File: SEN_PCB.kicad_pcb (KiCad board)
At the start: 2 copper layers, 42.5 x 58.7 mm, 8 parts, among them J1 47080-4005, U1 BME680, U2 ADT7310

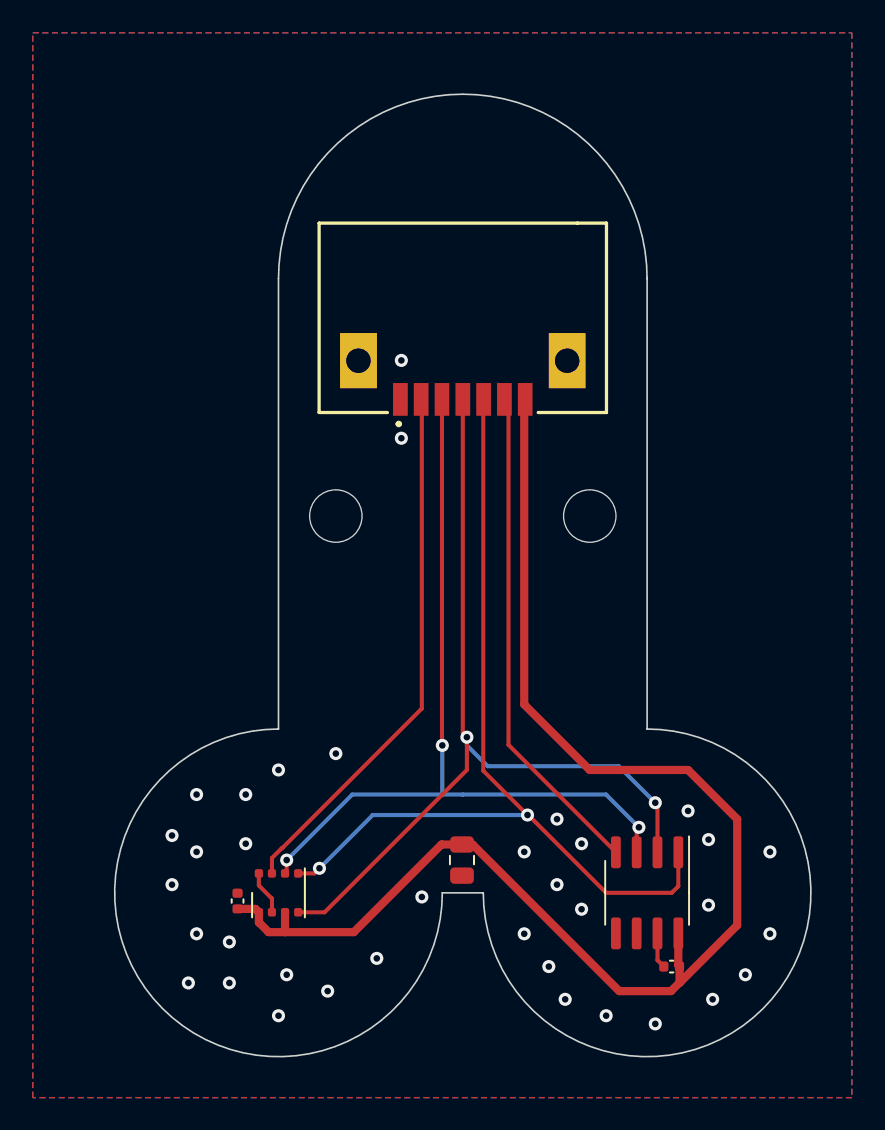
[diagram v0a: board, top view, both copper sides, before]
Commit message: 1V KiCad
Changed form-factor to more appropriate one.
Changed connector pinout meaning to match new pinout on MCU board.
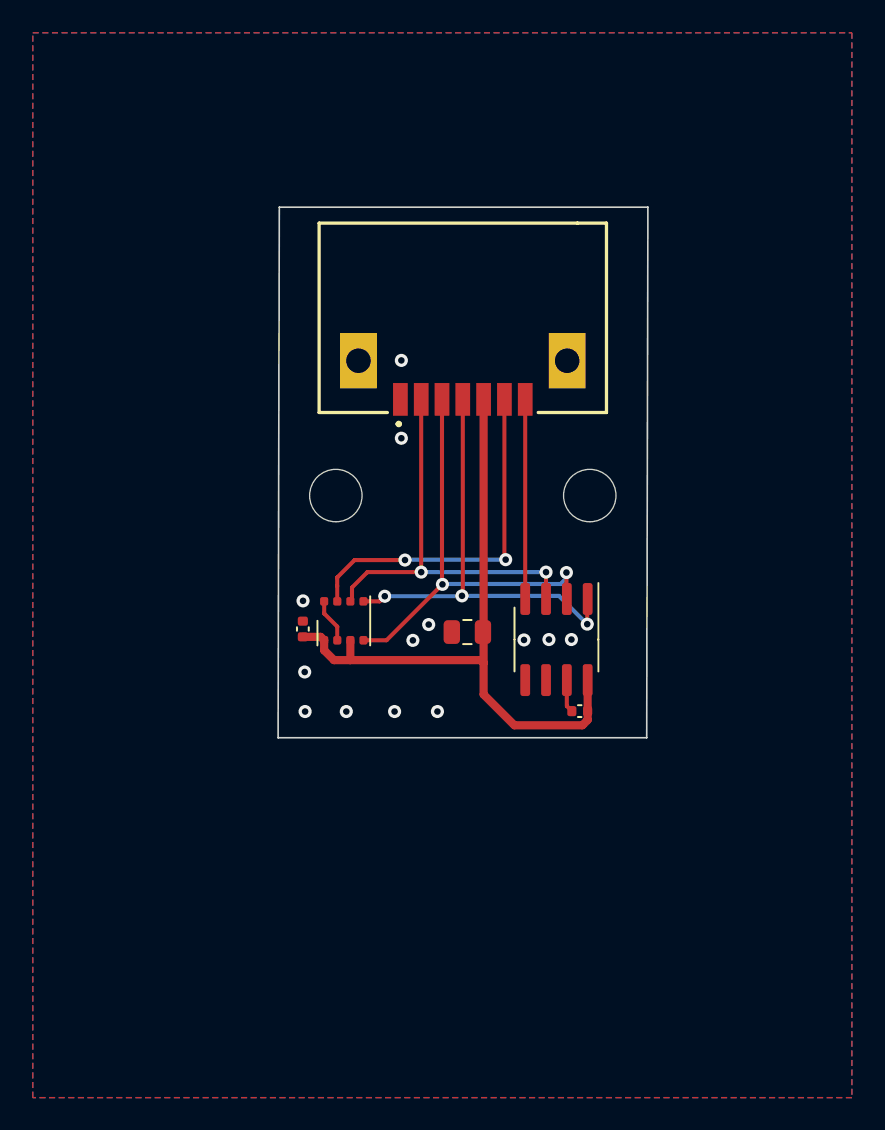
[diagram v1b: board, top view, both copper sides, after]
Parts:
- moved C1 17.1 mm to (66.5, 76.4)
- moved U1 17.1 mm to (69.0, 75.9)
- moved C2 16.6 mm to (83.4, 81.4)
- moved U2 16.4 mm to (82.0, 77.0)
- moved C3 13.9 mm to (76.5, 76.6), turned to 180 degrees
- moved H1 1.25 mm to (84.0, 68.2)
- moved H2 1.25 mm to (68.5, 68.2)
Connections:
- J1 pad 2: /BME_SS -> /MOSI
- J1 pad 3: /MOSI -> /MISO
- J1 pad 4: /MISO -> /CLK
- J1 pad 5: /CLK -> +3.3V
- J1 pad 6: /TEMP_SS -> /BME_SS
- J1 pad 7: +3.3V -> /TEMP_SS
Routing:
- net +3.3V: track 84.0 -> 41.0 mm
- net /CLK: track 55.5 -> 28.4 mm, vias 2 -> 3
- net /MISO: track 53.5 -> 27.2 mm
- net /MOSI: track 50.5 -> 25.3 mm, vias 3 -> 2
- net /TEMP_SS: track 30.4 -> 12.0 mm
- net /BME_SS: track 32.5 -> 22.0 mm, vias 0 -> 2
- net GND: track 4.89 -> 4.73 mm, vias 36 -> 13
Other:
- board size 42.5 x 58.7 mm -> 22.6 x 32.4 mm
- board text added: "MADE BY BASEMENT PROJECT WASSUP SENS BOARD V1"
